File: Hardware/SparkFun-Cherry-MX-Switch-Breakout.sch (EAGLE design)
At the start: 17 parts

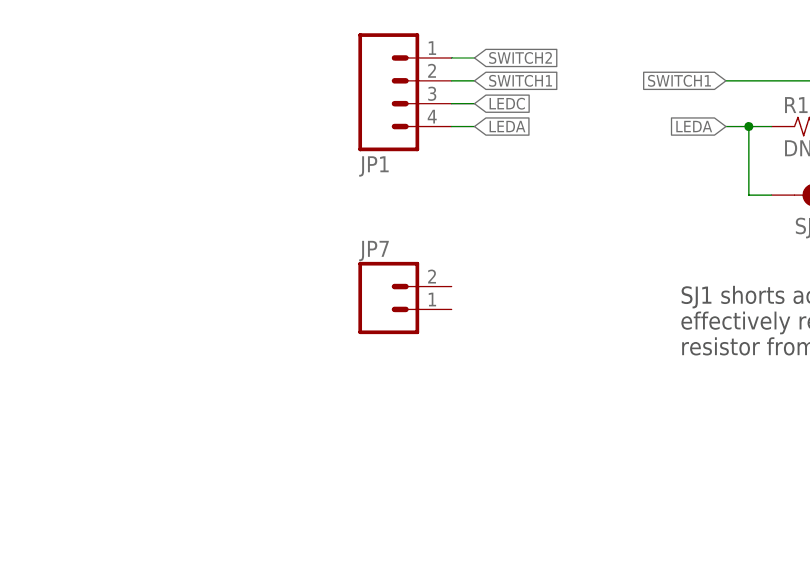
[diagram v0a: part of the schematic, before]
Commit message: Removing extra 2-pin connector.
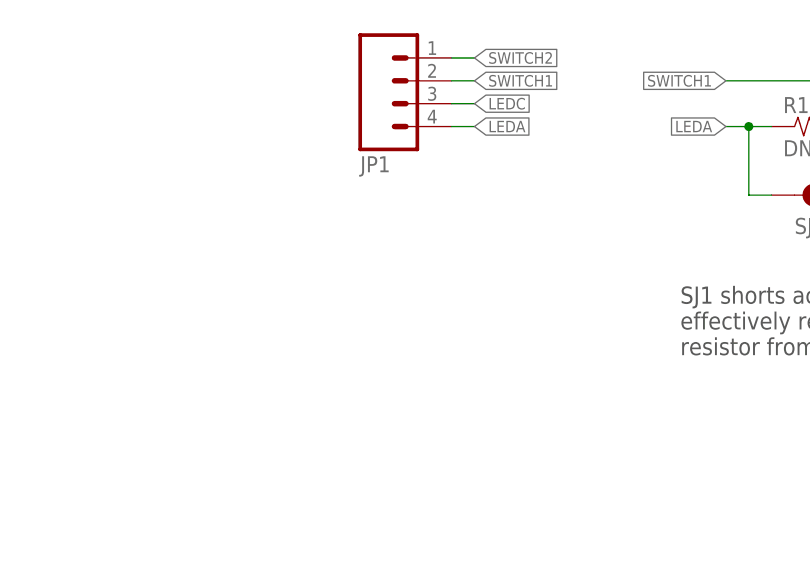
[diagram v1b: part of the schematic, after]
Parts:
- removed JP7: (no value), SparkFun-Connectors:M021X02_NO_SILK
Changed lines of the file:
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@@
 <grid distance="0.1" unitdist="inch" unit="inch" style="lines" multiple="1" display="no" altdistance="0.01" altunitdist="inch" altunit="inch"/>
 <layers>
-<layer number="1" name="Top" color="4" fill="1" visible="yes" active="no"/>
-<layer number="2" name="Route2" color="1" fill="3" visible="yes" active="no"/>
-<layer number="3" name="Route3" color="4" fill="3" visible="yes" active="no"/>
-<layer number="4" name="Route4" color="1" fill="4" visible="yes" active="no"/>
-<layer number="5" name="Route5" color="4" fill="4" visible="yes" active="no"/>
-<layer number="6" name="Route6" color="1" fill="8" visible="yes" active="no"/>
-<layer number="7" name="Route7" color="4" fill="8" visible="yes" active="no"/>
-<layer number="8" name="Route8" color="1" fill="2" visible="yes" active="no"/>
-<layer number="9" name="Route9" color="4" fill="2" visible="yes" active="no"/>
-<layer number="10" name="Route10" color="1" fill="7" visible="yes" active="no"/>
-<layer number="11" name="Route11" color="4" fill="7" visible="yes" active="no"/>
-<layer number="12" name="Route12" color="1" fill="5" visible="yes" active="no"/>
-<layer number="13" name="Route13" color="4" fill="5" visible="yes" active="no"/>
-<layer number="14" name="Route14" color="1" fill="6" visible="yes" active="no"/>
-<layer number="15" name="Route15" color="4" fill="6" visible="yes" active="no"/>
-<layer number="16" name="Bottom" color="1" fill="1" visible="yes" active="no"/>
-<layer number="17" name="Pads" color="2" fill="1" visible="yes" active="no"/>
-<layer number="18" name="Vias" color="2" fill="1" visible="yes" active="no"/>
-<layer number="19" name="Unrouted" color="6" fill="1" visible="yes" active="no"/>
-<layer number="20" name="Dimension" color="15" fill="1" visible="yes" active="no"/>
-<layer number="21" name="tPlace" color="16" fill="1" visible="yes" active="no"/>
-<layer number="22" name="bPlace" color="14" fill="1" visible="yes" active="no"/>
-<layer number="23" name="tOrigins" color="15" fill="1" visible="yes" active="no"/>
-<layer number="24" name="bOrigins" color="15" fill="1" visible="yes" active="no"/>
-<layer number="25" name="tNames" color="7" fill="1" visible="yes" active="no"/>
-<layer number="26" name="bNames" color="7" fill="1" visible="yes" active="no"/>
-<layer number="27" name="tValues" color="7" fill="1" visible="yes" active="no"/>
-<layer number="28" name="bValues" color="7" fill="1" visible="yes" active="no"/>
+<layer number="1" name="Top" color="4" fill="1" visible="no" active="no"/>
+<layer number="2" name="Route2" color="1" fill="3" visible="no" active="no"/>
+<layer number="3" name="Route3" color="4" fill="3" visible="no" active="no"/>
+<layer number="4" name="Route4" color="1" fill="4" visible="no" active="no"/>
+<layer number="5" name="Route5" color="4" fill="4" visible="no" active="no"/>
+<layer number="6" name="Route6" color="1" fill="8" visible="no" active="no"/>
+<layer number="7" name="Route7" color="4" fill="8" visible="no" active="no"/>
+<layer number="8" name="Route8" color="1" fill="2" visible="no" active="no"/>
+<layer number="9" name="Route9" color="4" fill="2" visible="no" active="no"/>
+<layer number="10" name="Route10" color="1" fill="7" visible="no" active="no"/>
+<layer number="11" name="Route11" color="4" fill="7" visible="no" active="no"/>
+<layer number="12" name="Route12" color="1" fill="5" visible="no" active="no"/>
+<layer number="13" name="Route13" color="4" fill="5" visible="no" active="no"/>
+<layer number="14" name="Route14" color="1" fill="6" visible="no" active="no"/>
+<layer number="15" name="Route15" color="4" fill="6" visible="no" active="no"/>
+<layer number="16" name="Bottom" color="1" fill="1" visible="no" active="no"/>
+<layer number="17" name="Pads" color="2" fill="1" visible="no" active="no"/>
+<layer number="18" name="Vias" color="2" fill="1" visible="no" active="no"/>
+<layer number="19" name="Unrouted" color="6" fill="1" visible="no" active="no"/>
+<layer number="20" name="Dimension" color="15" fill="1" visible="no" active="no"/>
+<layer number="21" name="tPlace" color="16" fill="1" visible="no" active="no"/>
+<layer number="22" name="bPlace" color="14" fill="1" visible="no" active="no"/>
+<layer number="23" name="tOrigins" color="15" fill="1" visible="no" active="no"/>
+<layer number="24" name="bOrigins" color="15" fill="1" visible="no" active="no"/>
+<layer number="25" name="tNames" color="7" fill="1" visible="no" active="no"/>
+<layer number="26" name="bNames" color="7" fill="1" visible="no" active="no"/>
+<layer number="27" name="tValues" color="7" fill="1" visible="no" active="no"/>
+<layer number="28" name="bValues" color="7" fill="1" visible="no" active="no"/>
 <layer number="29" name="tStop" color="7" fill="3" visible="no" active="no"/>
 <layer number="30" name="bStop" color="7" fill="6" visible="no" active="no"/>
@@
 <layer number="35" name="tGlue" color="7" fill="4" visible="no" active="no"/>
 <layer number="36" name="bGlue" color="7" fill="5" visible="no" active="no"/>
-<layer number="37" name="tTest" color="7" fill="1" visible="yes" active="no"/>
-<layer number="38" name="bTest" color="7" fill="1" visible="yes" active="no"/>
+<layer number="37" name="tTest" color="7" fill="1" visible="no" active="no"/>
+<layer number="38" name="bTest" color="7" fill="1" visible="no" active="no"/>
 <layer number="39" name="tKeepout" color="4" fill="11" visible="no" active="no"/>
 <layer number="40" name="bKeepout" color="1" fill="11" visible="no" active="no"/>
@@
 <layer number="44" name="Drills" color="7" fill="1" visible="no" active="no"/>
 <layer number="45" name="Holes" color="7" fill="1" visible="no" active="no"/>
-<layer number="46" name="Milling" color="3" fill="1" visible="yes" active="no"/>
-<layer number="47" name="Measures" color="7" fill="1" visible="yes" active="no"/>
-<layer number="48" name="Document" color="7" fill="1" visible="yes" active="no"/>
-<layer number="49" name="Reference" color="7" fill="1" visible="yes" active="no"/>
-<layer number="50" name="dxf" color="7" fill="1" visible="yes" active="no"/>
-<layer number="51" name="tDocu" color="6" fill="1" visible="yes" active="no"/>
-<layer number="52" name="bDocu" color="7" fill="1" visible="yes" active="no"/>
-<layer number="53" name="tGND_GNDA" color="7" fill="9" visible="yes" active="no"/>
-<layer number="54" name="bGND_GNDA" color="1" fill="9" visible="yes" active="no"/>
-<layer number="56" name="wert" color="7" fill="1" visible="yes" active="no"/>
-<layer number="57" name="tCAD" color="7" fill="1" visible="yes" active="no"/>
-<layer number="59" name="tCarbon" color="7" fill="1" visible="yes" active="no"/>
-<layer number="60" name="bCarbon" color="7" fill="1" visible="yes" active="no"/>
+<layer number="46" name="Milling" color="3" fill="1" visible="no" active="no"/>
+<layer number="47" name="Measures" color="7" fill="1" visible="no" active="no"/>
+<layer number="48" name="Document" color="7" fill="1" visible="no" active="no"/>
+<layer number="49" name="Reference" color="7" fill="1" visible="no" active="no"/>
+<layer number="50" name="dxf" color="7" fill="1" visible="no" active="no"/>
+<layer number="51" name="tDocu" color="6" fill="1" visible="no" active="no"/>
+<layer number="52" name="bDocu" color="7" fill="1" visible="no" active="no"/>
+<layer number="53" name="tGND_GNDA" color="7" fill="9" visible="no" active="no"/>
+<layer number="54" name="bGND_GNDA" color="1" fill="9" visible="no" active="no"/>
+<layer number="56" name="wert" color="7" fill="1" visible="no" active="no"/>
+<layer number="57" name="tCAD" color="7" fill="1" visible="no" active="no"/>
+<layer number="59" name="tCarbon" color="7" fill="1" visible="no" active="no"/>
+<layer number="60" name="bCarbon" color="7" fill="1" visible="no" active="no"/>
 <layer number="90" name="Modules" color="5" fill="1" visible="yes" active="yes"/>
 <layer number="91" name="Nets" color="2" fill="1" visible="yes" active="yes"/>
@@
 <part name="STANDOFF2" library="cherry-temp" deviceset="STAND-OFF" device="2-56"/>
 <part name="STANDOFF1" library="cherry-temp" deviceset="STAND-OFF" device="2-56"/>
-<part name="JP7" library="SparkFun-Connectors" deviceset="M02" device="1X02_NO_SILK"/>
 </parts>
 <sheets>
@@
 <instance part="STANDOFF2" gate="G$1" x="246.38" y="25.4"/>
 <instance part="STANDOFF1" gate="G$1" x="243.84" y="25.4"/>
-<instance part="JP7" gate="G$1" x="50.8" y="81.28"/>
 </instances>
 <busses>

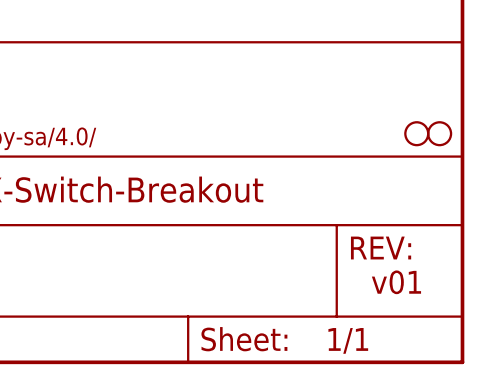
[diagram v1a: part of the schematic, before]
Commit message: Adjsting some silk, setting version to v10.
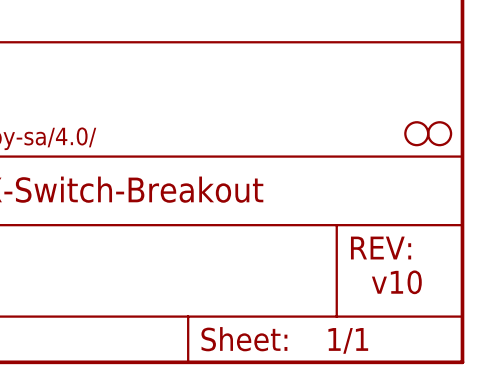
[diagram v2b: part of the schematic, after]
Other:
- note added: "v10"
- note removed: "v01"
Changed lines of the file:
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@@
 <?xml version="1.0" encoding="utf-8"?>
 <!DOCTYPE eagle SYSTEM "eagle.dtd">
-<eagle version="7.1.0">
+<eagle version="7.5.0">
 <drawing>
 <settings>
@@
 <sheet>
 <plain>
-<text x="238.76" y="7.62" size="2.54" layer="94">v01</text>
+<text x="238.76" y="7.62" size="2.54" layer="94">v10</text>
 <text x="171.45" y="11.43" size="2.54" layer="94">Jim Lindblom</text>
 <text x="83.82" y="83.82" size="1.905" layer="97" align="top-left">SJ1 shorts across R1,
